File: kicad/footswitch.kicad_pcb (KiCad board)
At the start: 2 copper layers, 100 x 100 mm, 72 parts, among them IC1 ATMEGA328P-A, P1 Atmega right, P2 Atmega top, P3 Programming header, P4 Atmega bottom, P5 Atmega left, P6 Pot hdr, P7 App select, Q1 BSS214NWH6327XTSA1, Q2 BSS214NWH6327XTSA1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

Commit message: Continue routing
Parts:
- BT1: footprint BC2AAPC:BC2AAPC -> Pin_Headers:Pin_Header_Straight_1x02_Pitch2.54mm
- C10, C11, C3, C6, C8, C9, D1, L1, Q1, Q2, R1, R10, R11, R2, R25, R26, RG1: moved to B.Cu
- moved SW4 181.4 mm to (142.0, 27.8)
- moved R11 180.5 mm to (52.0, 62.9)
- moved R26 179.0 mm to (52.0, 60.6)
- moved C15 147.7 mm to (85.0, 65.5)
- moved Q2 126.3 mm to (56.7, 61.9), turned to 270 degrees
- moved Q1 125.5 mm to (56.7, 57.0), turned to 270 degrees
- moved R10 124.1 mm to (52.0, 58.3)
- moved R25 122.7 mm to (52.0, 56.0)
- moved BT1 110.4 mm to (24.5, 65.5), turned to 270 degrees
- moved SW3 103.5 mm to (76.2, 57.5), turned to 90 degrees
- moved SW2 101.0 mm to (76.2, 61.2), turned to 90 degrees
- moved C16 82.1 mm to (85.0, 70.4)
- moved R3 44.4 mm to (73.4, 75.1)
- moved R20 44.2 mm to (51.4, 77.1), turned to 90 degrees
- moved C3 44.0 mm to (41.5, 62.2), turned to 0 degrees
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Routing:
- net RESET: track 25.4 -> 69.9 mm, vias 1 -> 0
- net Net-(AFF1-Pad13): track 0.00 -> 40.7 mm
- net Net-(AFF1-Pad14): track 0.00 -> 38.7 mm
- net SCL: track 16.7 -> 51.3 mm, vias 1 -> 0
- net D9: track 9.42 -> 42.2 mm
- net D8: track 17.3 -> 49.4 mm, vias 1 -> 0
- net D10: track 10.1 -> 38.7 mm
- net SDA: track 37.2 -> 63.1 mm, vias 1 -> 0
- net A2: track 32.6 -> 58.2 mm, vias 1 -> 0
- net A1: track 23.8 -> 43.1 mm, vias 1 -> 0
- net D3: track 21.4 -> 7.31 mm, vias 1 -> 0
- net 3V3: track 39.1 -> 52.7 mm
- net A3: track 33.7 -> 46.3 mm, vias 1 -> 0
- net VCC: track 14.4 -> 25.2 mm
- net A6: track 16.7 -> 11.7 mm, vias 1 -> 0
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
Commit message: Finish routing; markings and mounting still missing
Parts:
- removed SW4: SW_SPDT, switches:100SP4T1B1M1QEH
- C1, C4, R4, R5: moved to B.Cu
- moved C12 203.4 mm to (36.0, 53.5), turned to 180 degrees
- moved R5 193.9 mm to (36.1, 56.7), turned to 180 degrees
- moved C14 185.0 mm to (36.0, 56.0), turned to 180 degrees
- moved P3 143.5 mm to (74.8, 54.9), turned to 90 degrees
- moved R4 139.6 mm to (36.0, 53.3), turned to 180 degrees
- moved U1 132.0 mm to (40.0, 58.0)
- moved P6 103.3 mm to (81.3, 58.8), turned to 90 degrees
- moved RV1 94.8 mm to (81.3, 62.5), turned to 90 degrees
- moved P7 88.2 mm to (101.0, 84.5), turned to 90 degrees
- moved C2 24.5 mm to (47.2, 69.8), turned to 90 degrees
- moved C5 24.1 mm to (47.2, 76.8), turned to 270 degrees
- moved C1 22.8 mm to (45.5, 73.5), turned to 270 degrees
- moved C4 20.2 mm to (43.2, 73.5), turned to 270 degrees
- moved L1 17.3 mm to (52.8, 75.0)
- moved IC1 16.8 mm to (54.5, 69.8)
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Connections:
- C12 pad 1: VCC -> 3V3
- C14 pad 1: VCC -> 3V3
- R5 pad 2: VCC -> 3V3
- U1 pad 2: VCC -> 3V3
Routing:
- net Earth: track 10.2 -> 296.1 mm, vias 0 -> 14
- net 3V3: track 52.7 -> 204.4 mm, vias 0 -> 5
- net D3: track 7.31 -> 108.6 mm, vias 0 -> 2
- net D4: track 24.5 -> 122.4 mm, vias 0 -> 1
- net D2: track 10.2 -> 101.7 mm, vias 0 -> 2
- net D5: track 28.6 -> 112.8 mm, vias 0 -> 2
- net D8: track 49.4 -> 131.7 mm, vias 0 -> 1
- net SDA: track 63.1 -> 130.5 mm, vias 0 -> 1
- net MISO: track 11.6 -> 68.9 mm
- net SCK: track 9.25 -> 66.3 mm
- net A3: track 46.3 -> 100.9 mm, vias 0 -> 3
- net A6: track 11.7 -> 61.7 mm, vias 0 -> 4
- net TXO: track 9.49 -> 58.5 mm
- net D6: track 10.7 -> 56.3 mm, vias 0 -> 1
- net MOSI: track 10.9 -> 56.2 mm, vias 0 -> 1
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- added copper zone on B.Cu, net Earth
- added copper zone on F.Cu, net Earth
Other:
- board size 100 x 100 mm -> 81 x 35.7 mm

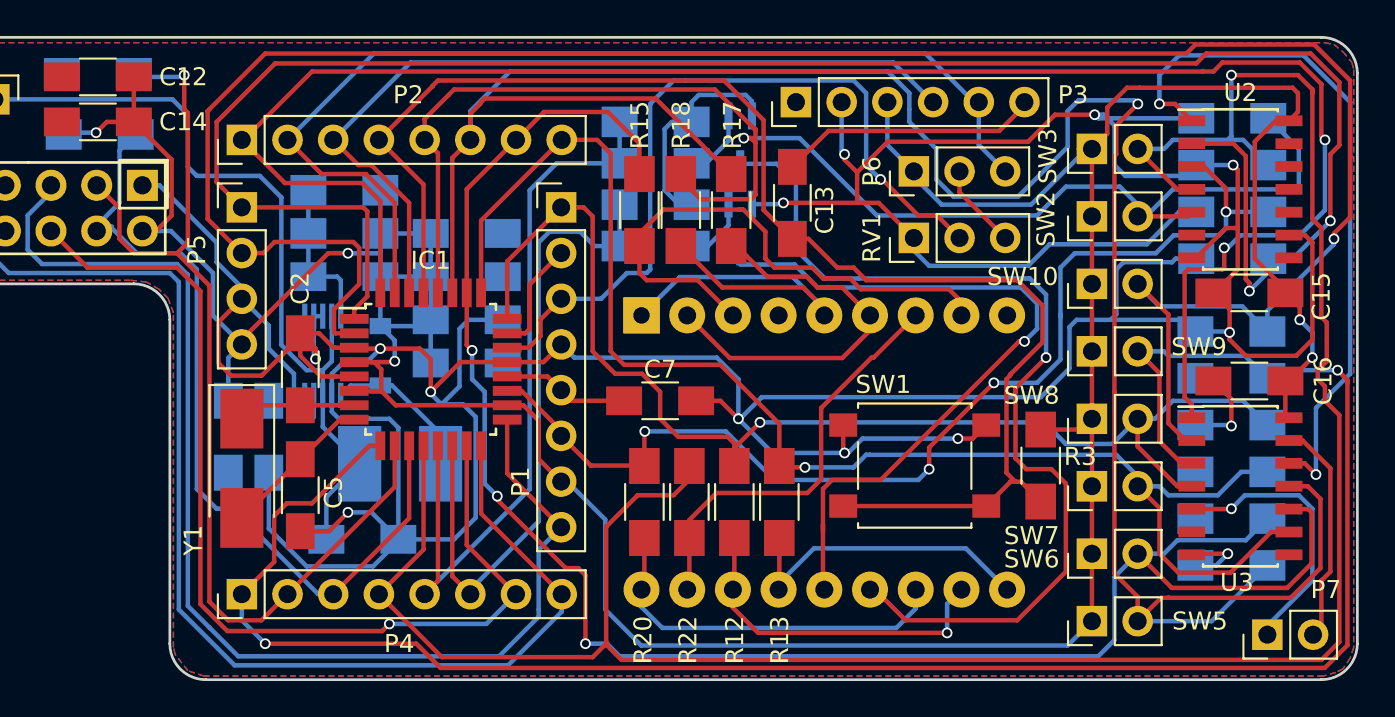
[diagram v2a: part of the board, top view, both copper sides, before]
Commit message: Remove OR gates; add version and authors to silk screen
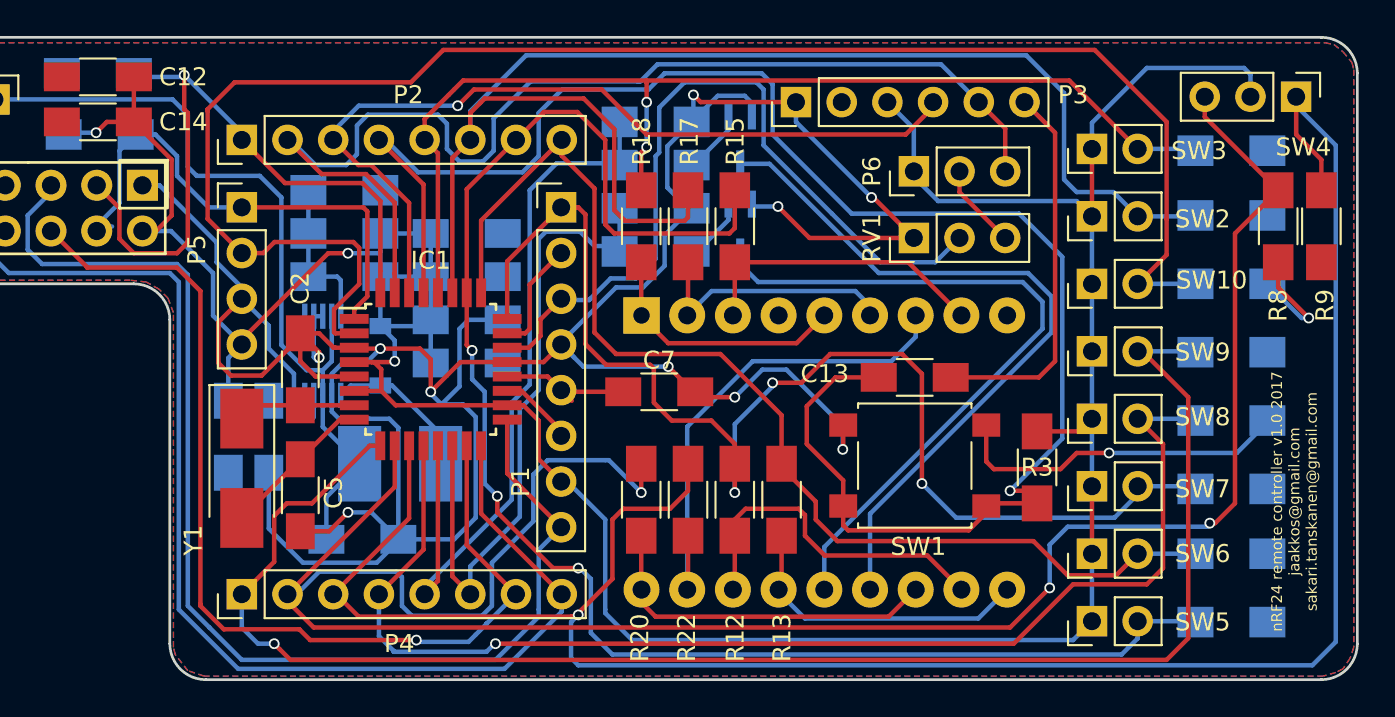
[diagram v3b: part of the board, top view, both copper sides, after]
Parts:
- removed C15, C16: 10uF, Capacitors_SMD:C_1206_HandSoldering
- removed P7: App select, Pin_Headers:Pin_Header_Straight_1x02_Pitch2.54mm
- removed U2, U3: CD4072BM96, Housings_SOIC:SOIC-14_3.9x8.7mm_Pitch1.27mm
- added SW4: SW_SPDT, Pin_Headers:Pin_Header_Straight_1x03_Pitch2.54mm, F.Cu at (102.6, 54.6)
- R8, R9: moved to F.Cu
- moved C13 11.8 mm to (81.4, 70.2), turned to 0 degrees
- moved R6 5.40 mm to (99.0, 61.2), turned to 180 degrees
- moved R15 5.38 mm to (71.4, 61.8)
- moved R9 5.27 mm to (104.0, 61.8), turned to 90 degrees
- moved R24 3.15 mm to (99.0, 83.8), turned to 180 degrees
- moved R8 2.67 mm to (101.6, 61.8), turned to 90 degrees
- moved R14 2.65 mm to (99.0, 65.0), turned to 180 degrees
- moved R17 2.56 mm to (68.8, 61.8)
- moved R18 2.38 mm to (66.2, 61.8)
- moved R23 1.95 mm to (99.0, 80.0), turned to 180 degrees
- moved R16 1.45 mm to (99.0, 68.8), turned to 180 degrees
- moved R21 0.95 mm to (99.0, 76.4), turned to 180 degrees
- moved R7 0.80 mm to (99.0, 57.6), turned to 180 degrees
- moved C7 0.50 mm to (67.2, 71.0)
- moved R11 0.30 mm to (67.0, 63.2)
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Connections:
- R19 pad 2: A1 -> D8
- R20 pad 2: A6 -> D6
- R21 pad 2: A2 -> A1
- R22 pad 2: D8 -> D7
- R23 pad 2: A3 -> A2
- R24 pad 2: SDA -> A3
- R4 pad 1: D6 -> D2
- R5 pad 1: D7 -> D3
- R6 pad 2: SCL -> SDA
- R7 pad 2: D8 -> SCL
- R8 pad 2: A6 -> D6
- R9 pad 2: D3 -> D7
- SW2 pad 2: SCL -> SDA
- SW3 pad 2: D8 -> SCL
- SW5 pad 2: SDA -> A3
- SW6 pad 2: A3 -> A2
- SW7 pad 2: A2 -> A1
- SW8 pad 2: A1 -> D8
- U1 pad 3: D6 -> D2
- U1 pad 4: D7 -> D3
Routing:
- net Earth: track 296.1 -> 211.1 mm, vias 14 -> 12
- net D3: track 108.6 -> 27.9 mm, vias 2 -> 0
- net D7: track 44.4 -> 120.0 mm, vias 0 -> 1
- net D6: track 56.3 -> 125.0 mm, vias 1 -> 3
- net D2: track 101.7 -> 39.3 mm, vias 2 -> 1
- net D8: track 131.7 -> 69.6 mm
- net A6: track 61.7 -> 4.46 mm, vias 4 -> 0
- net SDA: track 130.5 -> 79.6 mm, vias 1 -> 0
- net Net-(U2-Pad1): track 39.2 -> 0.00 mm, vias 2 -> 0
- net D4: track 122.4 -> 91.4 mm, vias 1 -> 0
- net 3V3: track 204.4 -> 180.2 mm, vias 5 -> 3
- net D5: track 112.8 -> 88.8 mm, vias 2 -> 1
- net RESET: track 78.8 -> 98.9 mm, vias 0 -> 1
- net SCL: track 82.0 -> 62.1 mm, vias 1 -> 2
- net A2: track 79.8 -> 63.6 mm, vias 1 -> 0
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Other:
- board text added: "nRF24 remote controller v1.0 2017 jaakkos@gmail.com sakari.tanskanen@gmail.com"

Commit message: Move boost converter inductor away from under Atmega
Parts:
- moved C11 5.18 mm to (51.6, 74.1)
- moved L1 3.36 mm to (51.5, 78.1)
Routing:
- net Earth: track 211.1 -> 194.3 mm
- net Net-(D1-Pad2): track 8.55 -> 12.6 mm
- net VCC: track 45.2 -> 43.1 mm
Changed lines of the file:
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@@
     (thickness 1.6)
     (drawings 13)
-    (tracks 803)
+    (tracks 798)
     (zones 0)
     (modules 67)
@@
     (tags "capacitor 1206")
     (attr smd)
-    (fp_text reference C7 (at 0 -1.75) (layer F.SilkS)
+    (fp_text reference C7 (at 0.1 1.8) (layer F.SilkS)
       (effects (font (size 1 1) (thickness 0.15)))
     )
@@
   )
   (module Capacitors_SMD:C_1206_HandSoldering (layer B.Cu)
-    (at 50.7 79.2)
+    (at 51.6 74.1)
     (descr "Capacitor SMD 1206, hand soldering")
     (tags "capacitor 1206")
@@
   )
   (module Inductors:Inductor_Taiyo-Yuden_NR-50xx_HandSoldering (layer B.Cu)
-    (at 52.8 75 180)
+    (at 51.5 78.1 180)
     (descr "Inductor, Taiyo Yuden, NR series, Taiyo-Yuden_NR-50xx, 4.9mmx4.9mm")
     (tags "inductor taiyo-yuden nr smd")
@@
   (segment (start 79.4 64.4) (end 87.7 64.4) (width 0.25) (layer B.Cu) (net 9))
   (segment (start 73.33 58.33) (end 79.4 64.4) (width 0.25) (layer B.Cu) (net 9))
-  (segment (start 48.7 76.85) (end 50.55 75) (width 0.25) (layer B.Cu) (net 10))
-  (segment (start 48.7 79.2) (end 48.7 76.85) (width 0.25) (layer B.Cu) (net 10))
-  (segment (start 48.5 72.95) (end 50.55 75) (width 0.25) (layer B.Cu) (net 10))
+  (segment (start 49.25 78.1) (end 49.25 74.45) (width 0.25) (layer B.Cu) (net 10))
+  (segment (start 49.25 74.45) (end 49.6 74.1) (width 0.25) (layer B.Cu) (net 10))
+  (segment (start 48.5 72.95) (end 48.5 73) (width 0.25) (layer B.Cu) (net 10))
   (segment (start 48.5 71.2) (end 48.5 72.95) (width 0.25) (layer B.Cu) (net 10))
+  (segment (start 48.5 73) (end 49.6 74.1) (width 0.25) (layer B.Cu) (net 10))
   (segment (start 49 66.8) (end 49 69.3) (width 0.25) (layer B.Cu) (net 10))
   (segment (start 49 69.3) (end 48.5 69.8) (width 0.25) (layer B.Cu) (net 10))
@@
   (segment (start 46.2 68.4) (end 47.6 69.8) (width 0.25) (layer B.Cu) (net 10))
   (segment (start 48.5 69.8) (end 48.5 71.2) (width 0.25) (layer B.Cu) (net 10))
+  (segment (start 53.6 74.1) (end 52.7 74.1) (width 0.25) (layer B.Cu) (net 11))
+  (segment (start 52.7 74.1) (end 51.1 72.5) (width 0.25) (layer B.Cu) (net 11))
+  (segment (start 46.7 80.6) (end 46.7 76.7) (width 0.25) (layer B.Cu) (net 11))
+  (segment (start 47.25 80.05) (end 46.7 80.6) (width 0.25) (layer F.Cu) (net 11))
+  (via (at 46.7 80.6) (size 0.6) (drill 0.4) (layers F.Cu B.Cu) (net 11))
+  (segment (start 47.25 78.75) (end 47.25 80.05) (width 0.25) (layer F.Cu) (net 11))
+  (segment (start 46.7 76.7) (end 45.5 75.5) (width 0.25) (layer B.Cu) (net 11))
+  (segment (start 45.5 75.5) (end 45.5 74.3) (width 0.25) (layer B.Cu) (net 11))
+  (segment (start 45.5 74.3) (end 47.2 72.6) (width 0.25) (layer B.Cu) (net 11))
   (segment (start 48.3 69.1) (end 48.3 68.8) (width 0.25) (layer F.Cu) (net 11))
   (segment (start 48.2 69.2) (end 48.3 69.1) (width 0.25) (layer B.Cu) (net 11))
@@
   (segment (start 54.5 69.2) (end 54.5 71) (width 0.25) (layer F.Cu) (net 11))
   (segment (start 53.9 68.6) (end 54.5 69.2) (width 0.25) (layer F.Cu) (net 11))
-  (segment (start 49.9 77.7) (end 51.2 77.7) (width 0.25) (layer B.Cu) (net 11))
-  (segment (start 47.25 78.75) (end 48.85 78.75) (width 0.25) (layer F.Cu) (net 11))
-  (via (at 49.9 77.7) (size 0.6) (drill 0.4) (layers F.Cu B.Cu) (net 11))
-  (segment (start 48.85 78.75) (end 49.9 77.7) (width 0.25) (layer F.Cu) (net 11))
-  (segment (start 51.2 77.7) (end 52.7 79.2) (width 0.25) (layer B.Cu) (net 11))
-  (segment (start 55.1 71.7) (end 56.3 71.7) (width 0.25) (layer B.Cu) (net 11))
-  (segment (start 55.8 79.2) (end 52.7 79.2) (width 0.25) (layer B.Cu) (net 11))
-  (segment (start 57 78) (end 55.8 79.2) (width 0.25) (layer B.Cu) (net 11))
-  (segment (start 57 72.4) (end 57 78) (width 0.25) (layer B.Cu) (net 11))
-  (segment (start 56.3 71.7) (end 57 72.4) (width 0.25) (layer B.Cu) (net 11))
-  (segment (start 52.7 73) (end 52.7 79.2) (width 0.25) (layer B.Cu) (net 11))
   (segment (start 49 71.2) (end 49 72.1) (width 0.25) (layer B.Cu) (net 11))
   (segment (start 49 72.1) (end 49.4 72.5) (width 0.25) (layer B.Cu) (net 11))
   (segment (start 49.4 72.5) (end 51.1 72.5) (width 0.25) (layer B.Cu) (net 11))
   (segment (start 51.1 72.5) (end 51.1 72.5) (width 0.25) (layer B.Cu) (net 11))
-  (segment (start 51.1 72.5) (end 52.2 72.5) (width 0.25) (layer B.Cu) (net 11))
-  (segment (start 52.2 72.5) (end 52.7 73) (width 0.25) (layer B.Cu) (net 11))
   (segment (start 50.3 68.6) (end 50.25 68.55) (width 0.25) (layer F.Cu) (net 11))
   (segment (start 50.3 68.6) (end 51.8 68.6) (width 0.25) (layer F.Cu) (net 11))
@@
   (segment (start 39.424 59.524) (end 42.6 62.7) (width 0.25) (layer B.Cu) (net 11))
   (segment (start 38.476 59.524) (end 39.424 59.524) (width 0.25) (layer B.Cu) (net 11))
-  (segment (start 45.5 75.5) (end 45.5 78.6) (width 0.25) (layer B.Cu) (net 11))
-  (segment (start 51.5 80.5) (end 52.7 79.3) (width 0.25) (layer B.Cu) (net 11))
-  (segment (start 47.4 80.5) (end 51.5 80.5) (width 0.25) (layer B.Cu) (net 11))
-  (segment (start 45.5 78.6) (end 47.4 80.5) (width 0.25) (layer B.Cu) (net 11))
-  (segment (start 52.7 79.3) (end 52.7 79.2) (width 0.25) (layer B.Cu) (net 11))
-  (segment (start 52.4 79.2) (end 52.7 79.2) (width 0.25) (layer B.Cu) (net 11))
   (segment (start 48 71.2) (end 48 72.4) (width 0.25) (layer B.Cu) (net 11))
   (segment (start 45.5 67.33) (end 44 65.83) (width 0.25) (layer B.Cu) (net 11))
@@
   (segment (start 44 65.7) (end 44 65.83) (width 0.25) (layer B.Cu) (net 11))
   (segment (start 61.52 68.6) (end 61.75 68.37) (width 0.25) (layer F.Cu) (net 11))
+  (segment (start 55.1 71.7) (end 56.3 71.7) (width 0.25) (layer B.Cu) (net 11))
+  (segment (start 57 72.4) (end 57 78) (width 0.25) (layer B.Cu) (net 11))
+  (segment (start 56.3 71.7) (end 57 72.4) (width 0.25) (layer B.Cu) (net 11))
   (segment (start 81.35 58.75) (end 81.35 59.05) (width 0.25) (layer B.Cu) (net 12))
   (segment (start 81.35 59.05) (end 82.7 60.4) (width 0.25) (layer B.Cu) (net 12))
@@
   (segment (start 89.2 69.3) (end 89.2 56.6) (width 0.25) (layer F.Cu) (net 18))
   (segment (start 88.3 70.2) (end 89.2 69.3) (width 0.25) (layer F.Cu) (net 18))
-  (segment (start 55.05 73.35) (end 55.05 75) (width 0.25) (layer B.Cu) (net 19))
-  (segment (start 52.35 70.65) (end 55.05 73.35) (width 0.25) (layer B.Cu) (net 19))
-  (segment (start 51.7 70.65) (end 52.35 70.65) (width 0.25) (layer B.Cu) (net 19))
+  (segment (start 55.25 73.05) (end 55.25 76.6) (width 0.25) (layer B.Cu) (net 19))
+  (segment (start 51.7 70.65) (end 52.85 70.65) (width 0.25) (layer B.Cu) (net 19))
+  (segment (start 52.85 70.65) (end 55.25 73.05) (width 0.25) (layer B.Cu) (net 19))
+  (segment (start 55.25 76.6) (end 53.75 78.1) (width 0.25) (layer B.Cu) (net 19))
   (segment (start 51.7 70.65) (end 50.05 70.65) (width 0.25) (layer B.Cu) (net 19))
   (segment (start 50.05 70.65) (end 49.5 71.2) (width 0.25) (layer B.Cu) (net 19))

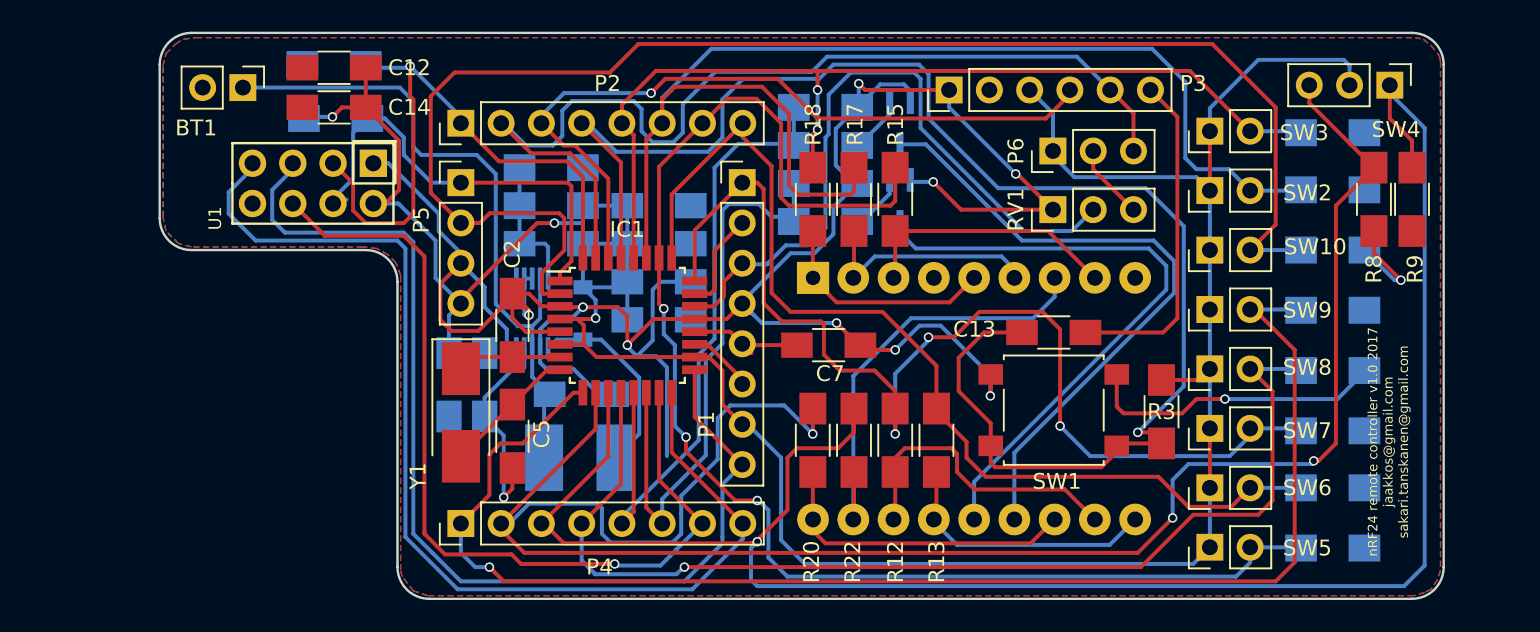
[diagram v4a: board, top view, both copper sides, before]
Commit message: Add mounting holes
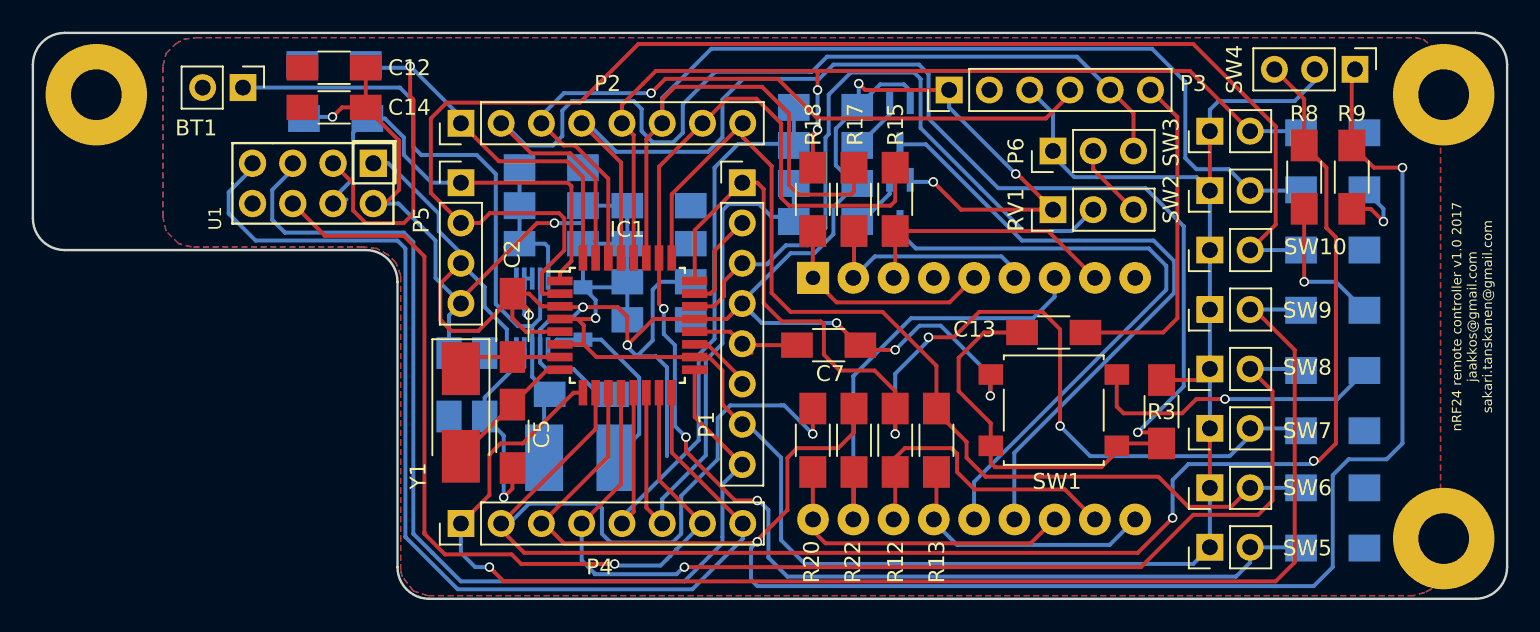
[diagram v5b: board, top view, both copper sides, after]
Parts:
- added REF**: MountingHole_3.2mm_M3_Pad, Mounting_Holes:MountingHole_3.2mm_M3_Pad, F.Cu at (21.0, 55.2)
- added REF**: MountingHole_3.2mm_M3_Pad, Mounting_Holes:MountingHole_3.2mm_M3_Pad, F.Cu at (106.0, 55.2)
- added REF**: MountingHole_3.2mm_M3_Pad, Mounting_Holes:MountingHole_3.2mm_M3_Pad, F.Cu at (106.0, 83.2)
- moved R8 4.62 mm to (97.2, 60.4)
- moved R9 4.05 mm to (100.2, 60.4)
- moved SW4 2.42 mm to (100.4, 53.6)
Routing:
- net Earth: track 194.3 -> 201.4 mm, vias 12 -> 13
- net D7: track 120.0 -> 114.3 mm, vias 1 -> 2
- net 3V3: track 180.2 -> 176.8 mm
- net D4: track 91.4 -> 89.8 mm
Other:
- board size 81 x 35.7 mm -> 93 x 35.7 mm
